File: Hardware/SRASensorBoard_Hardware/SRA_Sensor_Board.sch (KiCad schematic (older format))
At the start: 12 parts, among them U1 OKI-78SR-5_1.5-W36H-C, U2 OKI-78SR-3.3_1.5-W36H-C

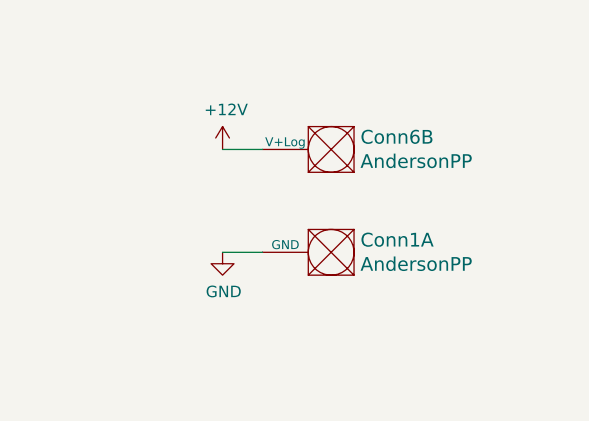
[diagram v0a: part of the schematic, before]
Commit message: fixed autosave files
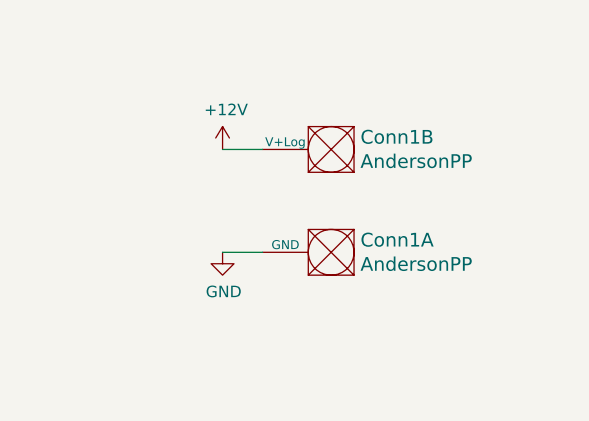
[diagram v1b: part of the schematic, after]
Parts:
- Conn1: renamed from Conn6; footprint MRDT_Connectors:Anderson_1_Horizontal -> MRDT_Connectors:Anderson_2_Horizontal_Side_by_Side
- Conn1: footprint MRDT_Connectors:Anderson_1_Horizontal -> MRDT_Connectors:Anderson_2_Horizontal_Side_by_Side
- R1: footprint Resistor_SMD:R_0402_1005Metric -> Resistor_SMD:R_0603_1608Metric_Pad1.05x0.95mm_HandSolder
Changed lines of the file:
@@
 $EndDescr
 $Comp
-L MRDT_Connectors:AndersonPP Conn6
+L MRDT_Connectors:AndersonPP Conn1
 U 2 1 614D19B3
 P 10275 950
-F 0 "Conn6" H 10247 997 60  0000 R CNN
+F 0 "Conn1" H 10247 997 60  0000 R CNN
 F 1 "AndersonPP" H 10247 1103 60  0000 R CNN
-F 2 "MRDT_Connectors:Anderson_1_Horizontal" H 10125 400 60  0001 C CNN
+F 2 "MRDT_Connectors:Anderson_2_Horizontal_Side_by_Side" H 10125 400 60  0001 C CNN
 F 3 "" H 10125 400 60  0001 C CNN
 	2    10275 950
@@
 F 0 "Conn1" H 10247 1447 60  0000 R CNN
 F 1 "AndersonPP" H 10247 1553 60  0000 R CNN
-F 2 "MRDT_Connectors:Anderson_1_Horizontal" H 10125 850 60  0001 C CNN
+F 2 "MRDT_Connectors:Anderson_2_Horizontal_Side_by_Side" H 10125 850 60  0001 C CNN
 F 3 "" H 10125 850 60  0001 C CNN
 	1    10275 1400
@@
 F 0 "R1" V 9943 5225 50  0000 C CNN
 F 1 "100" V 10034 5225 50  0000 C CNN
-F 2 "Resistor_SMD:R_0402_1005Metric" V 10080 5225 50  0001 C CNN
+F 2 "Resistor_SMD:R_0603_1608Metric_Pad1.05x0.95mm_HandSolder" V 10080 5225 50  0001 C CNN
 F 3 "~" H 10150 5225 50  0001 C CNN
 	1    10150 5225
